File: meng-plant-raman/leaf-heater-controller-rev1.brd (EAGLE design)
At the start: 20.3 x 10.2 mm, 4 parts, among them IC1 MAX30205MTA+, X1 SM06B-SRSS-TB

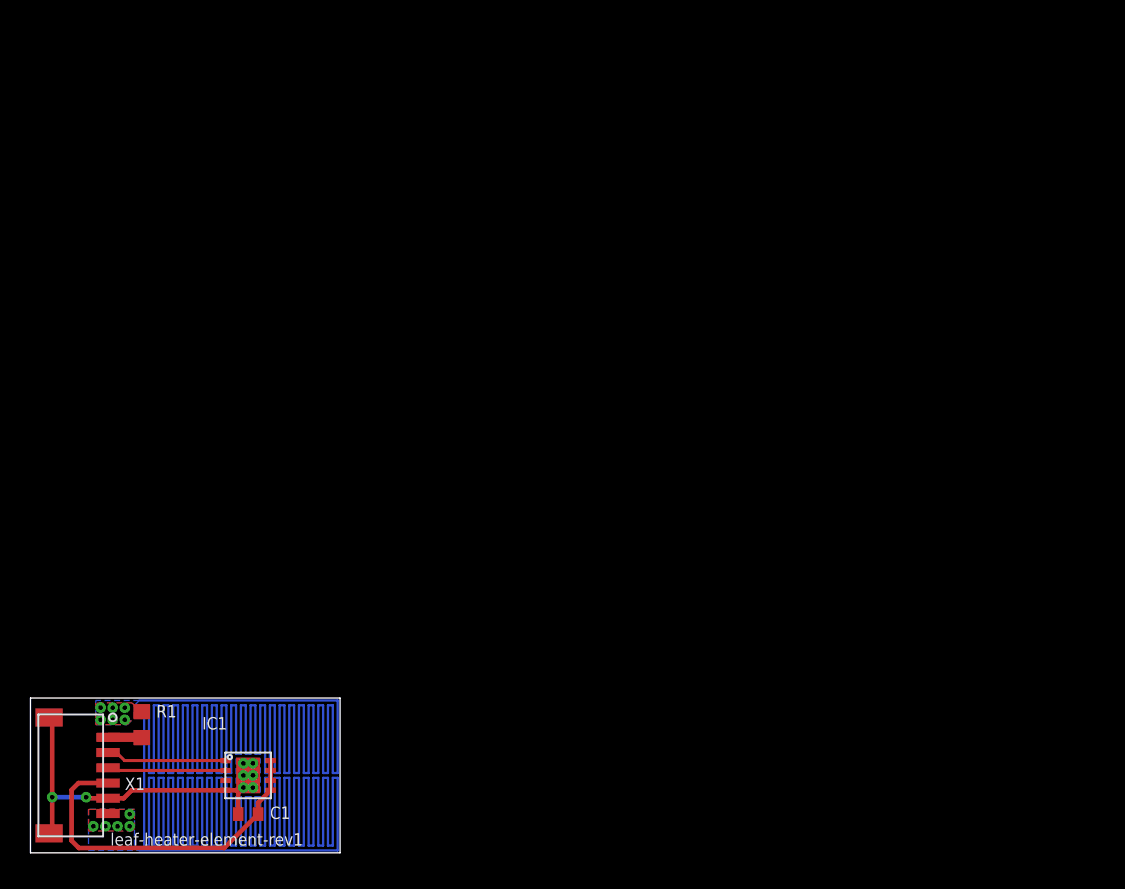
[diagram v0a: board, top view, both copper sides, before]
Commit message: Updated leaf heaters with 6-pin JST SH
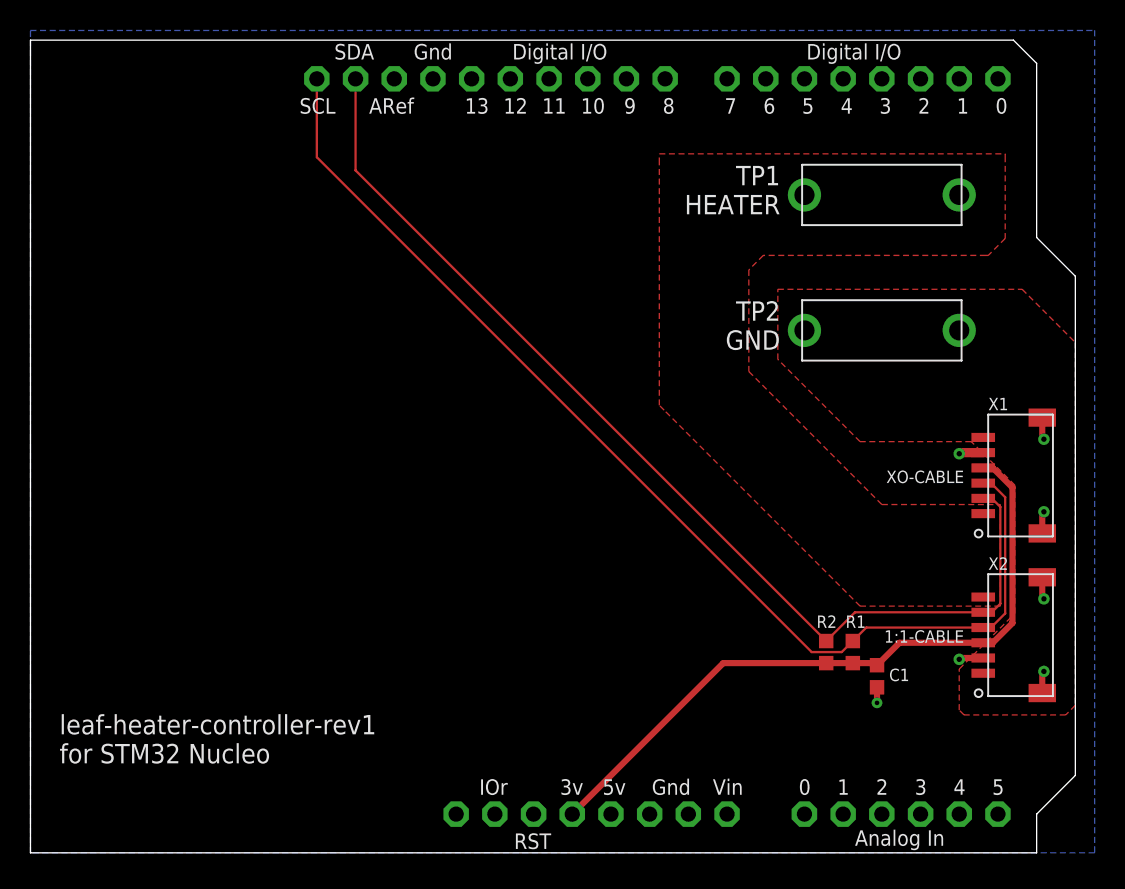
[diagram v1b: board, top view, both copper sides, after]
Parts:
- removed IC1: MAX30205MTA+, meng-plant-raman:TDFN-08
- added R2: 2k2, rcl-modified-footprints:R0603
- added TP1: 105-0752-001, meng-plant-raman:CINCH-BANANA-105-075X-001
- added TP2: 105-0753-001, meng-plant-raman:CINCH-BANANA-105-075X-001
- added U1: ARDUINOR3-DIMENSION, adafruit:ARDUINOR3
- added X2: SM06B-SRSS-TB, meng-plant-raman:JST-SM06B-SRSS-TB
- C1: device rcl:C0402 -> rcl-modified-footprints:C0603
- R1: value 0R -> 2k2; device rcl:R0603 -> rcl-modified-footprints:R0603
- moved X1 69.8 mm to (67.3, 24.8), turned to 90 degrees
- moved R1 46.9 mm to (54.0, 13.2)
- moved C1 42.3 mm to (55.6, 11.6), turned to 270 degrees
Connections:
- removed net NC_TEMP_OS: IC1.3
- removed net SENSOR_GND: C1.2, IC1.4, IC1.EXP, X1.5, X1.PAD1, X1.PAD2
- new net 5V: U1.5V
- new net GND1: U1.GND1
- new net GND2: U1.GND2
- new net HEATER_GND: TP2.1, TP2.2, X1.6, X2.1
- new net VIN: U1.VIN
- net GND: now also C1.2, U1.GND, X1.5, X1.PAD1, X1.PAD2, X2.2, X2.PAD1, X2.PAD2; no longer R1.1, X1.6
- net HEATER_VDD: now also TP1.1, TP1.2, X2.6; no longer R1.2
- net PP_P3V3_SENSOR: now also R1.2, R2.2, U1.3V, X2.3; no longer IC1.5, IC1.6, IC1.7, IC1.8
- net TEMP_SCL: now also R1.1, U1.SCL, X2.4; no longer IC1.2
- net TEMP_SDA: now also R2.1, U1.SDA, X2.5; no longer IC1.1
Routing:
- net GND: track 401.6 -> 10.1 mm, vias 11 -> 7
- net TEMP_SCL: track 7.79 -> 74.3 mm
- net TEMP_SDA: track 7.94 -> 69.8 mm
- net SENSOR_GND: track 22.5 -> 0.00 mm, vias 8 -> 0
- net PP_P3V3_SENSOR: track 23.1 -> 45.5 mm
- net HEATER_VDD: track 2.22 -> 0.00 mm
- added copper zone on layer 1, net HEATER_GND
- added copper zone on layer 1, net HEATER_VDD
- removed copper zone on layer 1, net GND
- removed copper zone on layer 16, net SENSOR_GND
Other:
- board size 20.3 x 10.2 mm -> 68.6 x 53.3 mm
- board text added: "1:1-CABLE"
- board text added: "GND"
- board text added: "HEATER"
- board text added: "XO-CABLE"
- board text added: "leaf-heater-controller-rev1 for STM32 Nucleo"
- board text removed: "leaf-heater-element-rev1"
